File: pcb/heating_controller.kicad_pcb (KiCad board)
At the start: 2 copper layers, 145 x 81 mm, 25 parts

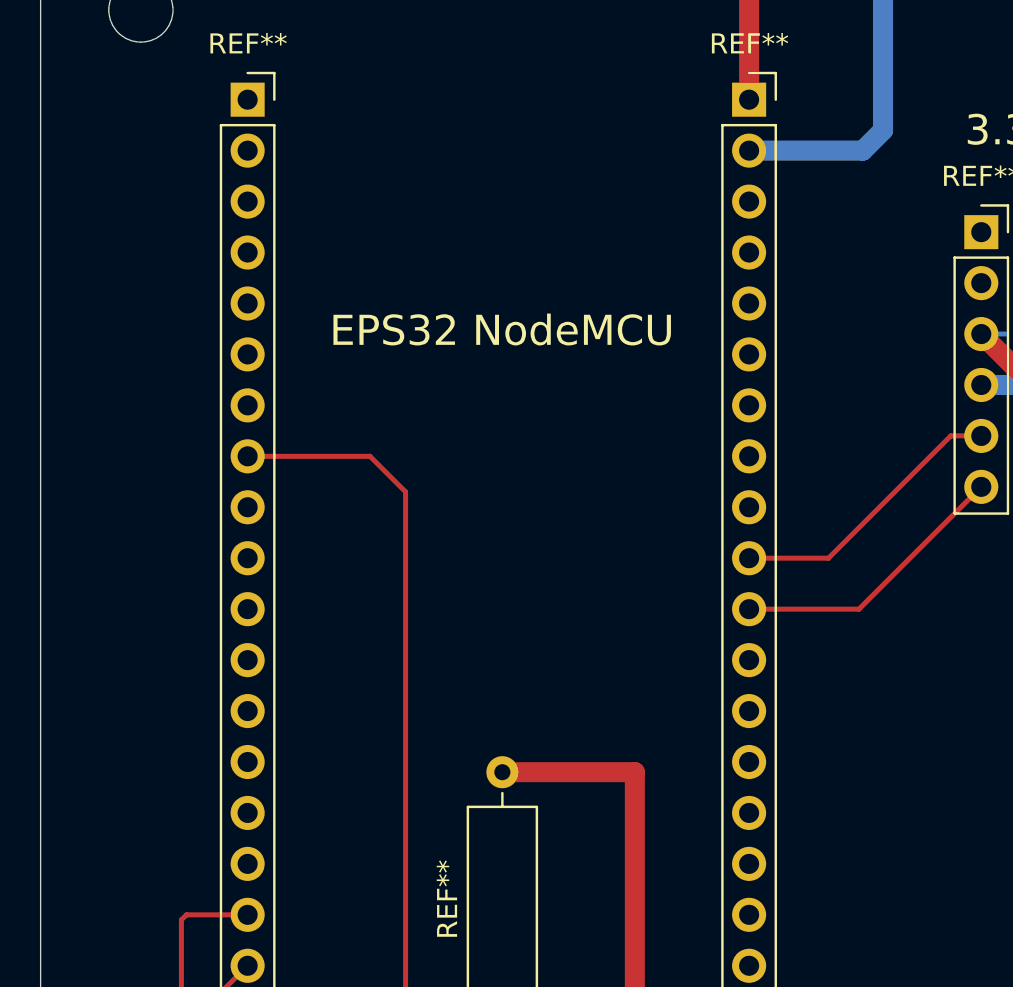
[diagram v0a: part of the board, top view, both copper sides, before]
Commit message: adding rxtx socket correct gnd connection on esp
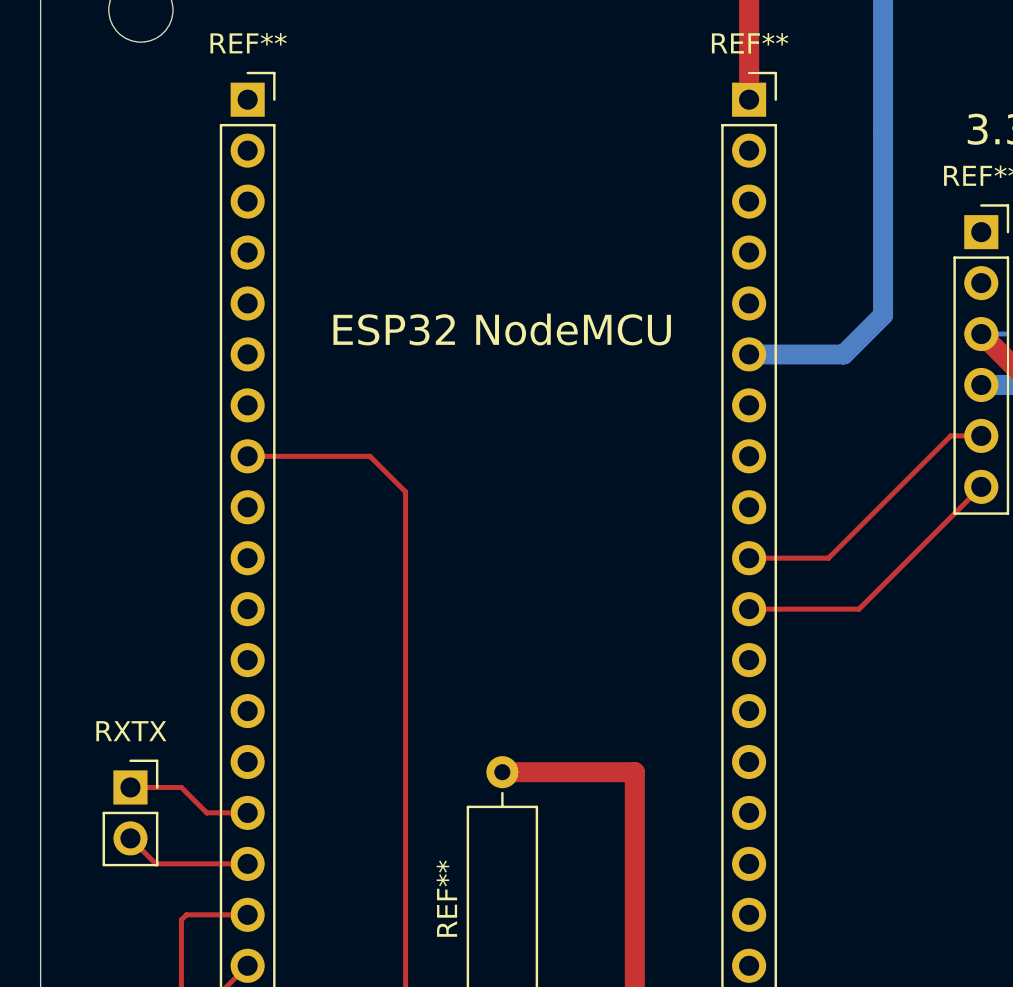
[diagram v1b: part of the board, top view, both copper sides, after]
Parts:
- added RXTX: PinSocket_1x02_P2.54mm_Vertical, Connector_PinSocket_2.54mm:PinSocket_1x02_P2.54mm_Vertical, F.Cu at (30.5, 111.8)
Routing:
- net (no net): track 1320.0 -> 1342.3 mm
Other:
- board text added: "ESP32 NodeMCU"
- board text removed: "EPS32 NodeMCU"
